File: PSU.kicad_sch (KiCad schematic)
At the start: 0 parts

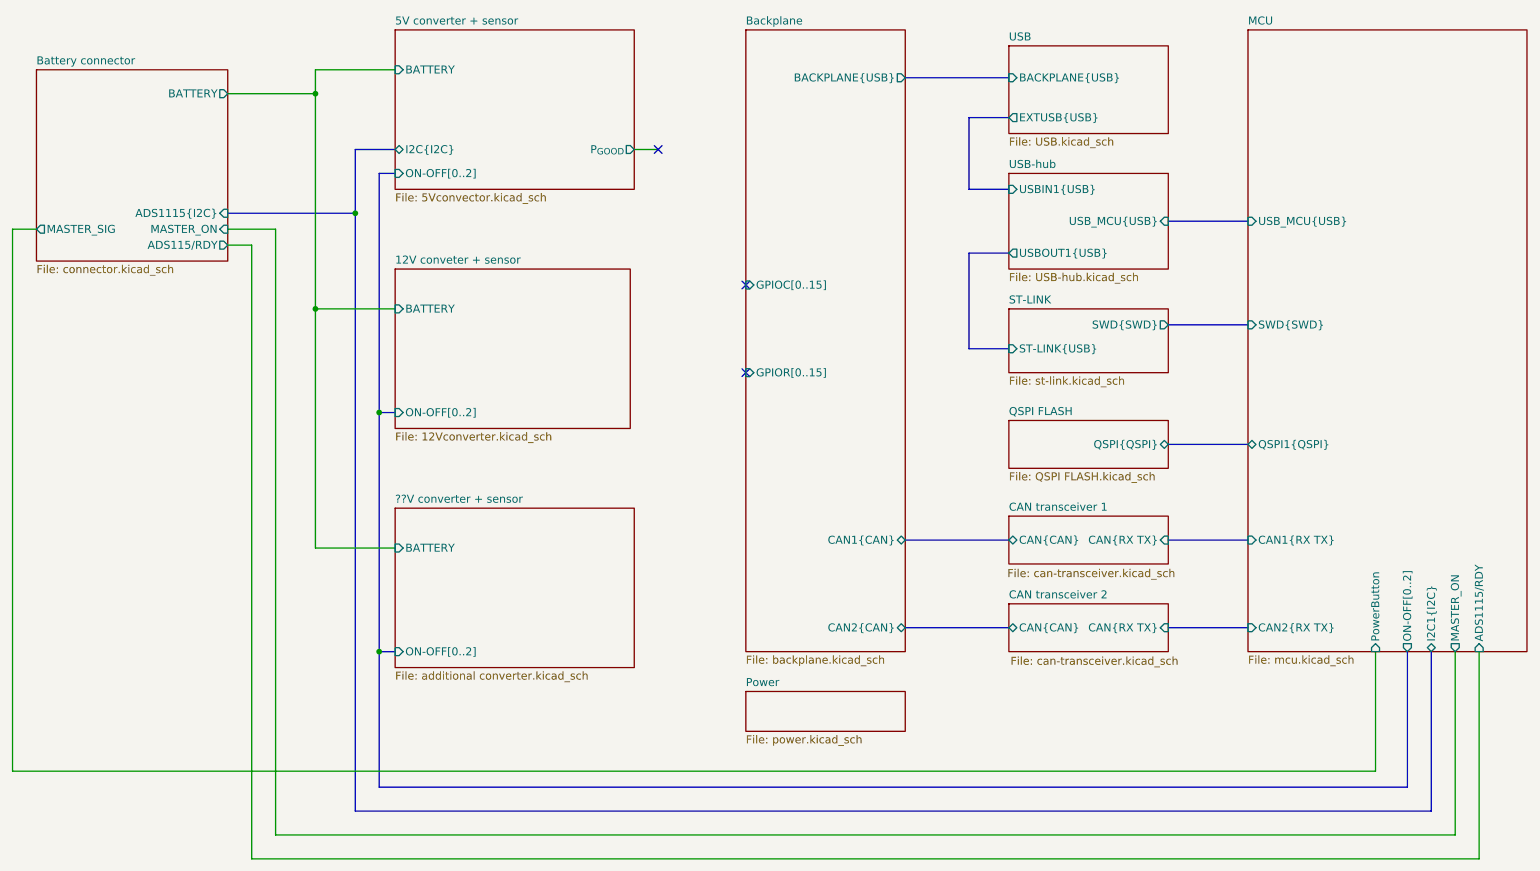
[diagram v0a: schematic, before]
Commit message: Change MCU to STM32H563
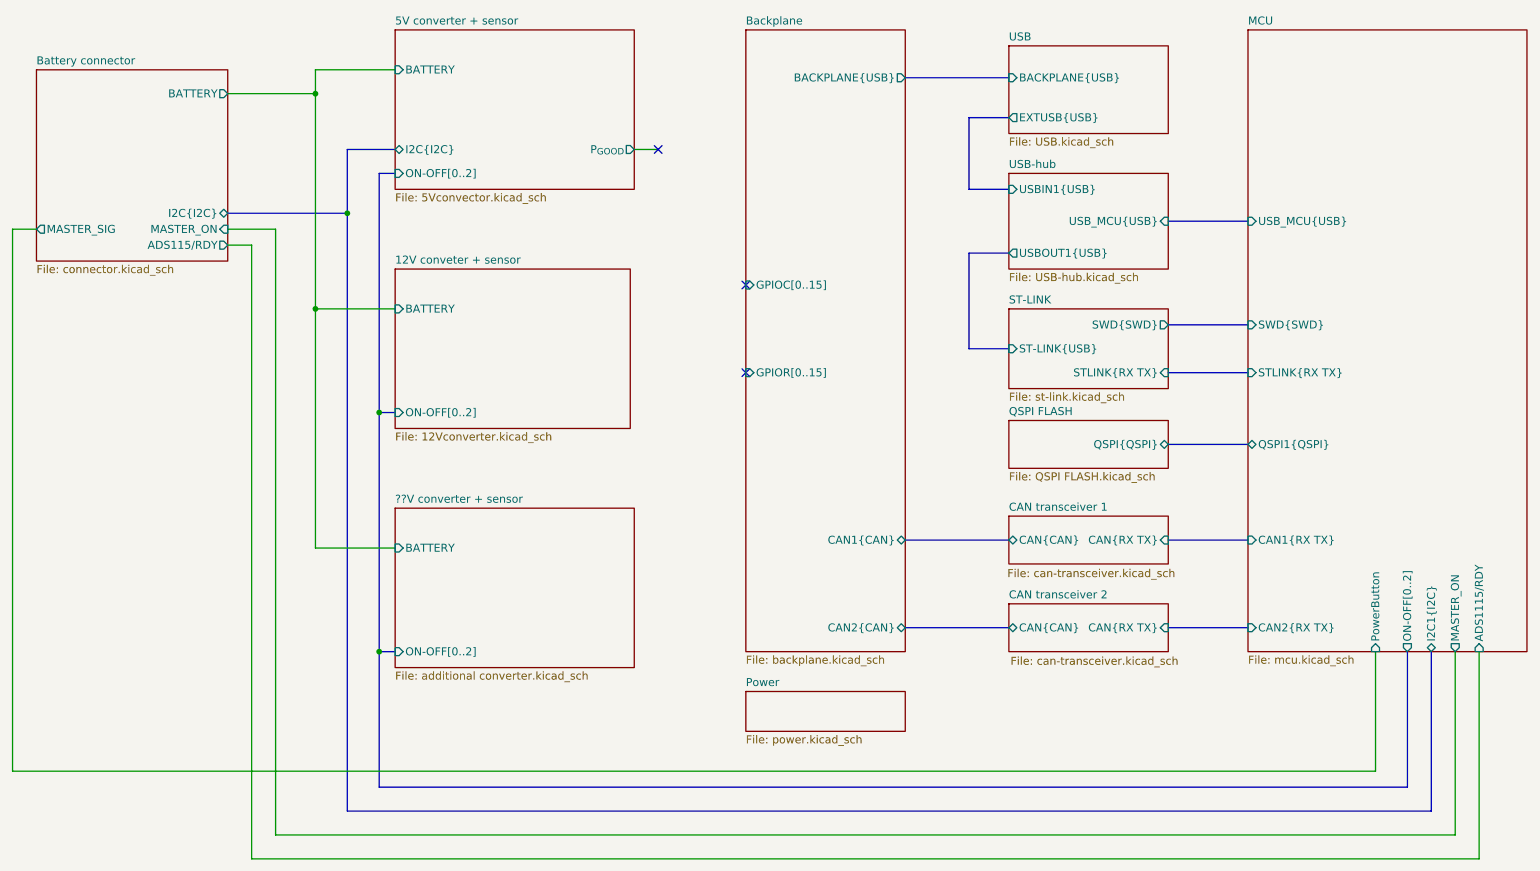
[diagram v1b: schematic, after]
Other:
- sheet Battery connector ports: added I2C{I2C}; removed ADS1115{I2C}
- sheet MCU ports: added STLINK{RX TX}; removed none
- sheet ST-LINK ports: added STLINK{RX TX}; removed none
